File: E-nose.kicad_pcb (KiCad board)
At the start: 2 copper layers, 34 parts, among them T1 Temp_si072, U1 TCA9548APWR, U3 RTC_DS3231

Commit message: Final with Gerbers
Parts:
- removed XA2: Arduino_Due_Shield, Arduino:Arduino_Due_Shield
- added ?: , , F.Cu at (175.8, 104.6)
- moved C1 101.3 mm to (122.5, 89.2), turned to 0 degrees
- moved U3 95.8 mm to (188.8, 64.8), turned to 270 degrees
- moved JP2 90.5 mm to (116.9, 96.5), turned to 270 degrees
- moved C2 89.5 mm to (123.2, 108.4), turned to 270 degrees
- moved R1 85.6 mm to (119.1, 94.8), turned to 90 degrees
- moved JP3 81.3 mm to (121.4, 96.3), turned to 90 degrees
- moved R2 80.8 mm to (123.7, 94.9), turned to 90 degrees
- moved R3 80.0 mm to (120.4, 108.5)
- moved MD7 79.3 mm to (180.0, 82.2), turned to 0 degrees
- moved U1 78.5 mm to (126.0, 102.0), turned to 270 degrees
- moved JP4 75.7 mm to (119.7, 105.2), turned to 0 degrees
- moved R6 73.2 mm to (106.3, 80.7), turned to 180 degrees
- moved R4 72.9 mm to (127.2, 92.9), turned to 90 degrees
- moved MD8 71.6 mm to (188.6, 82.1), turned to 0 degrees
- moved R5 70.8 mm to (107.4, 83.1), turned to 180 degrees
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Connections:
- MD3 pad 4: SC5 -> SC0
- MD3 pad 6: SD5 -> SD0
- MD4 pad 4: SC4 -> SC1
- MD4 pad 6: SD4 -> SD1
- MD5 pad 4: SC2 -> SC3
- MD5 pad 6: SD2 -> SD3
- MD6 pad 4: SC3 -> SC2
- MD6 pad 6: SD3 -> SD2
- MD7 pad 4: SC1 -> SC5
- MD7 pad 6: SD1 -> SD5
- MD8 pad 4: SC0 -> SC4
- MD8 pad 6: SD0 -> SD4
- XA1 pad 5V2: Net-(XA1-Pad5V2) -> +5V
- XA1 pad GND2: Net-(XA1-PadGND2) -> GND
- XA1 pad GND4: Net-(XA1-PadGND4) -> GND
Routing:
- net VCC: track 0.00 -> 334.4 mm, vias 0 -> 3
- net GND: track 0.00 -> 301.5 mm, vias 0 -> 2
- net I2C_DATA: track 0.00 -> 138.2 mm
- net I2C_CLK: track 0.00 -> 135.0 mm, vias 0 -> 1
- net SC4: track 0.00 -> 70.4 mm
- net SD4: track 0.00 -> 65.8 mm
- net +5V: track 0.00 -> 60.3 mm, vias 0 -> 1
- net SC5: track 0.00 -> 59.6 mm
- net SD5: track 0.00 -> 56.9 mm
- net SD6: track 0.00 -> 46.4 mm
- net SC6: track 0.00 -> 44.1 mm
- net SC2: track 0.00 -> 42.5 mm
- net SD2: track 0.00 -> 38.8 mm
- net SC3: track 0.00 -> 36.2 mm
- net SC7: track 0.00 -> 35.7 mm
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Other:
- board outline added: 101.6 x 53.4 mm
- board text added: "E-Nose DataLogger V1.0"

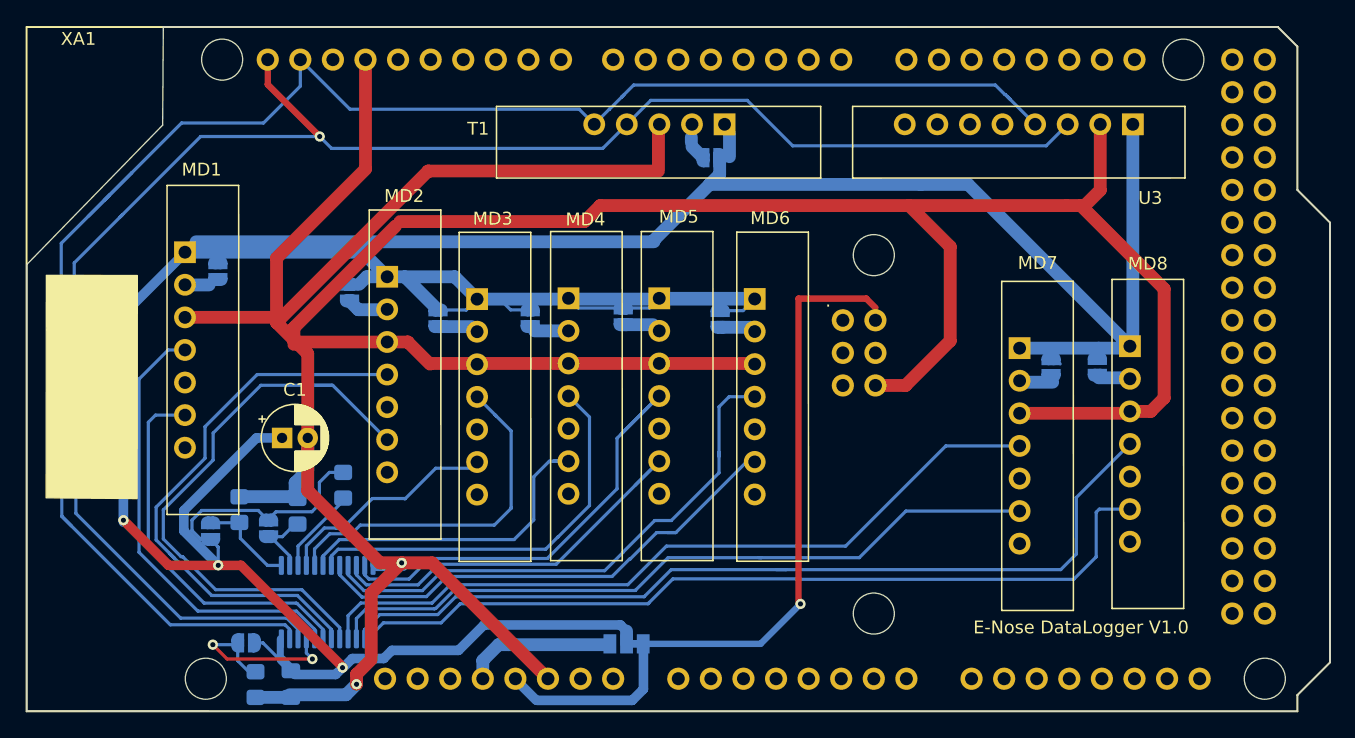
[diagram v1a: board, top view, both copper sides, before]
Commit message: Dip switch add
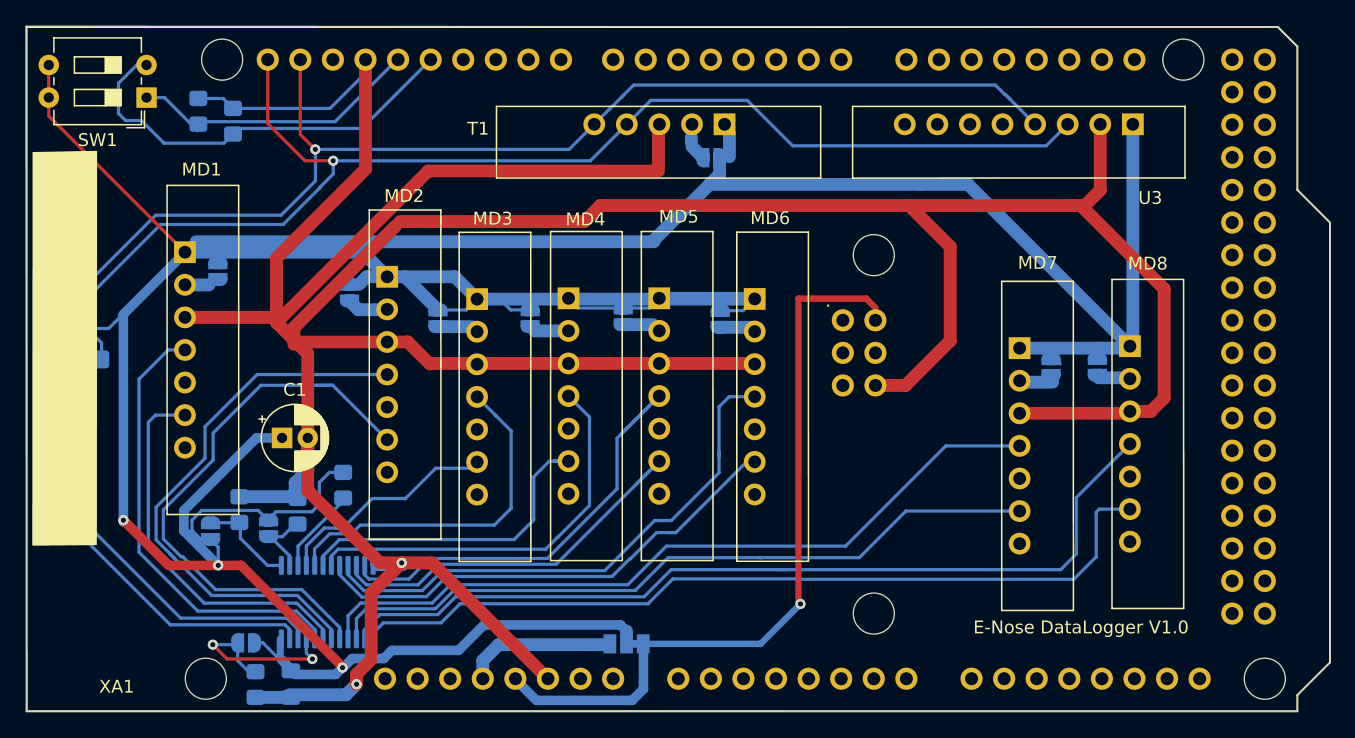
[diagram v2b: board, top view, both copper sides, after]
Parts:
- added R7: 10K, Resistor_SMD:R_0805_2012Metric_Pad1.20x1.40mm_HandSolder, B.Cu at (115.9, 63.8)
- added R8: 10K, Resistor_SMD:R_0805_2012Metric_Pad1.20x1.40mm_HandSolder, B.Cu at (118.6, 64.5)
- added SW1: SW_DIP_x02, Button_Switch_THT:SW_DIP_SPSTx02_Slide_6.7x6.64mm_W7.62mm_P2.54mm_LowProfile, F.Cu at (111.9, 62.7)
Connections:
- XA1 pad D12: Net-(XA1-PadD12) -> DIP2
- XA1 pad D13: Net-(XA1-PadD13) -> DIP1
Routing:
- net DIP2: track 0.00 -> 33.4 mm
- net DIP1: track 0.00 -> 23.0 mm
- net VCC: track 334.4 -> 353.4 mm
- net GND: track 301.5 -> 317.1 mm
- net I2C_DATA: track 138.2 -> 133.3 mm, vias 0 -> 1
- net I2C_CLK: track 135.0 -> 136.2 mm
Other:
- outline, holes or cut-outs redrawn
